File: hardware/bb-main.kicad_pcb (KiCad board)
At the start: 2 copper layers, 62 x 19 mm, 27 parts, among them P1 USB_B, P2 PICkit3, P3 OLED, SW1 SW_PUSH, U1 BU33TD3WG-TR, U2 PIC16(L)F1455-I/SL

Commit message: Board rework
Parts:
- added ?: , Housings_Proj:VIA-0.6mm, F.Cu at (91.2, 77.5)
- C1, C3, C4: footprint Capacitors_SMD:C_0603_HandSoldering -> Capacitors_SMD:C_0603
- C2: footprint Capacitors_Tantalum_SMD:TantalC_SizeA_EIA-3216_HandSoldering -> Capacitors_Tantalum_SMD:TantalC_SizeA_EIA-3216_Reflow
- D2: value L1 -> Led_Small
- moved R9 17.5 mm to (93.7, 72.1), turned to 0 degrees
- moved R1 17.3 mm to (80.3, 73.9), turned to 0 degrees
- moved R13 17.2 mm to (93.7, 77.5), turned to 0 degrees
- moved R12 16.2 mm to (93.7, 70.4), turned to 0 degrees
- moved R10 16.1 mm to (93.7, 75.7), turned to 0 degrees
- moved R11 16.1 mm to (93.7, 73.9), turned to 0 degrees
- moved SW1 14.4 mm to (85.1, 84.3)
- moved D1 13.7 mm to (66.1, 84.6)
- moved R5 13.5 mm to (93.7, 86.6)
- moved P2 13.0 mm to (81.0, 71.1), turned to 180 degrees
- moved R3 11.4 mm to (69.8, 84.6), turned to 180 degrees
- moved D2 8.86 mm to (57.7, 74.7), turned to 270 degrees
- moved R4 8.48 mm to (93.7, 79.5)
- moved R6 6.23 mm to (93.7, 81.3)
- moved R3.2 6.10 mm to (59.4, 74.1)
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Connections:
- P1 pad 5: Net-(P1-Pad5) -> (no net)
- P2 pad 6: Net-(P2-Pad6) -> (no net)
- P3 pad 5: GND -> /~RES~
- P3 pad 6: GND -> /~CS~
- P3 pad 7: /~RES~ -> GND
- P3 pad 8: /~CS~ -> GND
- U1 pad 4: Net-(U1-Pad4) -> (no net)
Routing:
- net +5V: track 0.71 -> 60.8 mm, vias 0 -> 2
- net +3V3: track 0.39 -> 51.0 mm, vias 0 -> 1
- net /ICSPDAT/OLED_SCK: track 0.45 -> 34.3 mm
- net /OLED_SDO: track 0.15 -> 25.5 mm, vias 0 -> 2
- net /OLED_~RES~: track 0.00 -> 20.4 mm
- net /OLED_D/~C~: track 0.15 -> 20.0 mm
- net /OLED_~CS~: track 1.15 -> 20.2 mm
- net /BUT_1: track 0.00 -> 16.7 mm
- net /SCK: track 13.5 -> 30.1 mm
- net /~RES~: track 13.7 -> 26.4 mm
- net /~MCLR~: track 1.92 -> 11.6 mm, vias 0 -> 2
- net GND: track 21.9 -> 13.2 mm, vias 2 -> 0
- net /LED_A: track 0.00 -> 7.69 mm
- net /SDO: track 13.5 -> 6.92 mm, vias 0 -> 1
- net /ICSPCLK: track 0.60 -> 6.77 mm
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- added copper zone on B.Cu, net GND
- added copper zone on F.Cu, net GND
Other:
- board size 62 x 19 mm -> 50.5 x 19 mm
- board text added: "Devs Build Button"
- board text added: "v1.0"

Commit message: Board changes
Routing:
- net /SDO: track 6.92 -> 8.95 mm
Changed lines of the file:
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@@
   (general
     (links 56)
-    (no_connects 15)
-    (area 54.949999 68.949999 105.550001 88.050001)
+    (no_connects 1)
+    (area 53.852999 68.949999 105.550001 88.413001)
     (thickness 1.6)
     (drawings 7)
-    (tracks 171)
+    (tracks 172)
     (zones 0)
     (modules 28)
@@
     (47 F.CrtYd user)
     (48 B.Fab user)
-    (49 F.Fab user)
+    (49 F.Fab user hide)
   )
   (setup
@@
       (net 1 GND) (zone_connect 2))
   )
-  (gr_text v1.0 (at 89.662 71.628) (layer F.Cu)
+  (gr_text v1.0 (at 91.694 67.183) (layer F.Cu)
     (effects (font (size 0.508 0.508) (thickness 0.127)))
   )
-  (gr_text "Devs Build Button" (at 86.995 70.485) (layer F.Cu)
+  (gr_text "Devs Build Button" (at 86.995 67.056) (layer F.Cu)
     (effects (font (size 1.27 0.508) (thickness 0.127)))
   )
@@
   (segment (start 68.207 78.46) (end 68.94 78.46) (width 0.254) (layer F.Cu) (net 2))
   (segment (start 68.94 78.46) (end 69.944 78.46) (width 0.254) (layer F.Cu) (net 2))
+  (segment (start 71.9582 73.025) (end 64.516 80.4672) (width 0.381) (layer B.Cu) (net 3))
   (segment (start 67.25751 69.71349) (end 65.278 71.693) (width 0.381) (layer F.Cu) (net 3))
   (segment (start 76.7334 73.025) (end 71.9582 73.025) (width 0.381) (layer B.Cu) (net 3))
-  (segment (start 71.9582 73.025) (end 64.516 80.4672) (width 0.381) (layer B.Cu) (net 3))
   (segment (start 78.486 71.2724) (end 76.7334 73.025) (width 0.381) (layer B.Cu) (net 3))
   (segment (start 78.486 71.2724) (end 78.486 71.12) (width 0.381) (layer B.Cu) (net 3))
@@
   (segment (start 70.866 71.2724) (end 70.866 71.12) (width 0.254) (layer F.Cu) (net 11))
   (segment (start 72.001001 72.407401) (end 70.866 71.2724) (width 0.254) (layer F.Cu) (net 11))
+  (segment (start 94.826 77.47) (end 94.826 79.502) (width 0.254) (layer F.Cu) (net 12))
   (segment (start 96.266 77.47) (end 99.06 74.676) (width 0.254) (layer B.Cu) (net 12))
   (segment (start 99.06 74.676) (end 100.584 74.676) (width 0.254) (layer B.Cu) (net 12))

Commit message: Board final rev 1.0
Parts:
- removed ?: , Housings_Proj:VIA-0.6mm
- moved R9 18.1 mm to (82.8, 86.6), turned to 180 degrees
- moved R5 17.1 mm to (77.5, 81.3)
- moved R6 16.4 mm to (77.5, 83.1)
- moved R8 16.4 mm to (77.5, 86.6)
- moved R7 16.4 mm to (77.5, 84.8)
- moved R4 16.3 mm to (77.5, 79.5)
- moved R12 15.4 mm to (82.8, 81.3), turned to 180 degrees
- moved R10 14.2 mm to (82.8, 84.8), turned to 180 degrees
- moved R11 14.2 mm to (82.8, 83.1), turned to 180 degrees
- moved R13 14.1 mm to (79.7, 77.7), turned to 180 degrees
- moved OLED 13.6 mm to (95.0, 85.6), turned to 180 degrees
- moved BTN 11.9 mm to (92.5, 74.9), turned to 90 degrees
- moved R3.2 6.72 mm to (65.5, 71.2)
- moved C2 6.37 mm to (58.6, 75.1)
- moved D2 6.31 mm to (63.9, 73.7)
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- renumbered SW1 to BTN, P3 to OLED, P1 to USB
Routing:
- net GND: track 13.2 -> 47.9 mm
- net /BUT_1: track 16.7 -> 32.7 mm, vias 0 -> 1
- net /ICSPDAT/OLED_SCK: track 34.3 -> 20.0 mm, vias 0 -> 1
- net /~RES~: track 26.4 -> 13.6 mm, vias 0 -> 1
- net /OLED_SDO: track 25.5 -> 14.4 mm, vias 2 -> 0
- net /SDO: track 8.95 -> 19.7 mm
- net /OLED_D/~C~: track 20.0 -> 9.83 mm
- net /OLED_~CS~: track 20.2 -> 10.3 mm
- net +5V: track 60.8 -> 50.9 mm, vias 2 -> 3
- net /OLED_~RES~: track 20.4 -> 10.8 mm
- net /~MCLR~: track 11.6 -> 16.6 mm, vias 2 -> 1
- net /SCK: track 30.1 -> 35.1 mm, vias 0 -> 1
- net Net-(P1-Pad3): track 8.00 -> 5.33 mm
- net Net-(P1-Pad2): track 8.19 -> 5.52 mm
- net /D/~C~: track 14.6 -> 16.6 mm, vias 0 -> 1
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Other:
- board size 50.5 x 19 mm -> 41.9 x 19 mm
- net class Default: trace_width 0.254 -> 0.2032
- net class Power: trace_width 0.381 -> 0.254
- rule via_min_size: 0.4 -> 0.3302
- board text added: "Button"
- board text added: "Devs Build"
- board text removed: "Devs Build Button"

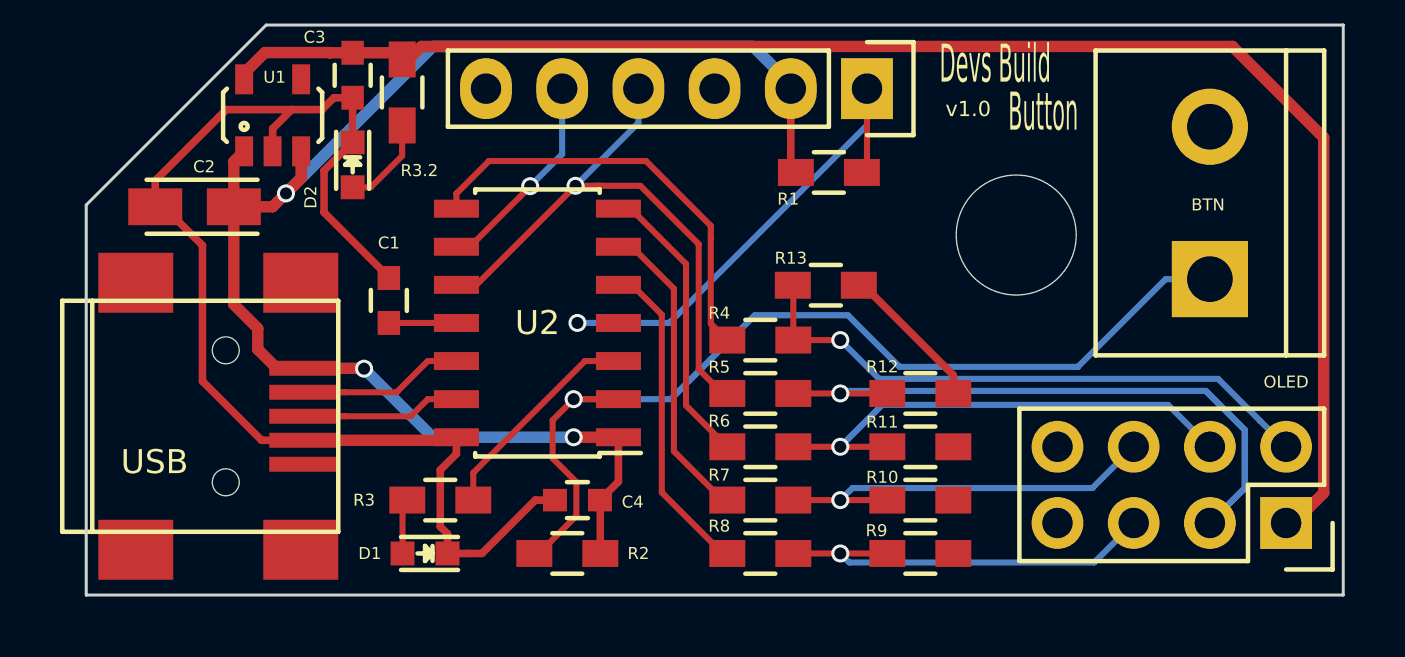
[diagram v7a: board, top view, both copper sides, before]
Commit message: Fix board unconnected track. Changed schematic USB connector.
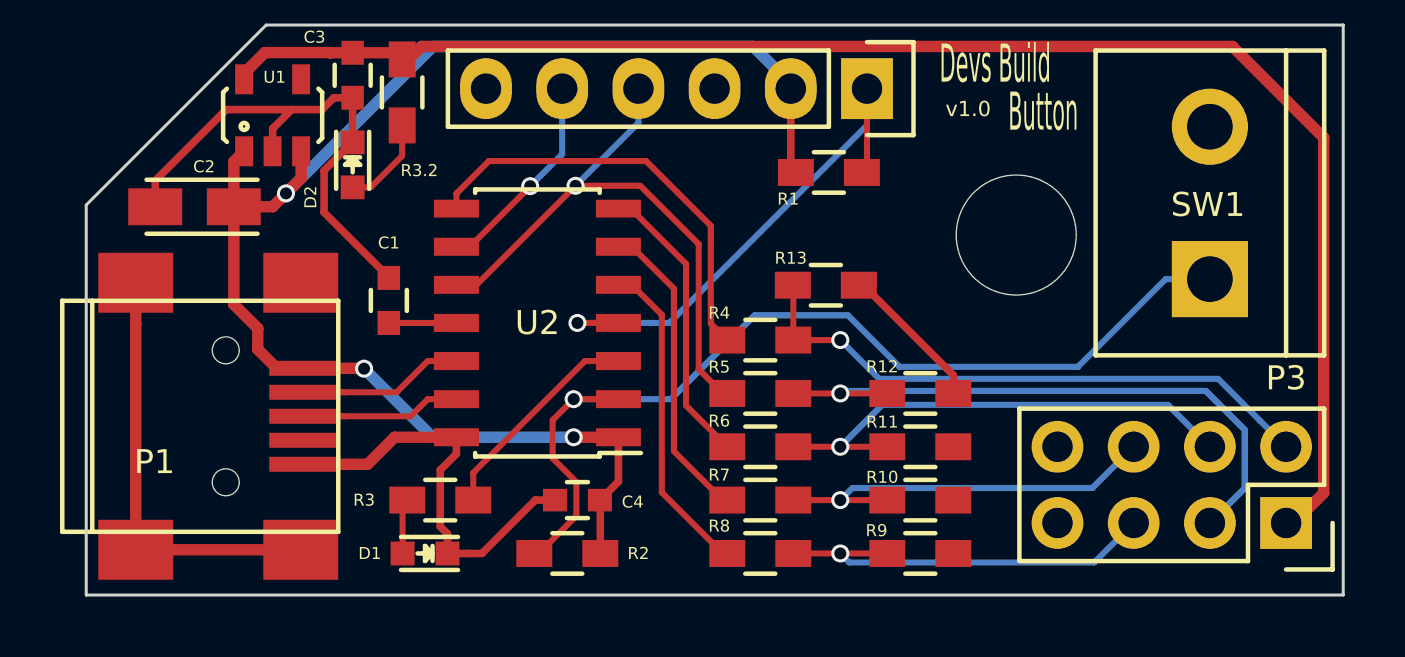
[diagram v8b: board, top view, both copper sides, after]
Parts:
- renumbered USB to P1, OLED to P3, BTN to SW1
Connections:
- P1 pad 4: GND -> Net-(P1-Pad4)
- P1 pad 5: (no net) -> GND
- P1 pad 6: (no net) -> GND
- P2 pad 6: (no net) -> Net-(P2-Pad6)
- U1 pad 4: (no net) -> Net-(U1-Pad4)
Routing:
- net GND: track 47.9 -> 52.3 mm
- net /~MCLR~: track 16.6 -> 18.0 mm
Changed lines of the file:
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@@
-(kicad_pcb (version 4) (host pcbnew 4.0.2-stable)
+(kicad_pcb (version 4) (host pcbnew 4.0.0-stable)
   (general
-    (links 55)
-    (no_connects 0)
-    (area 53.725999 68.090976 96.971001 88.050001)
+    (links 59)
+    (no_connects 11)
+    (area 54.949999 68.949999 96.951001 88.050001)
     (thickness 1.6)
     (drawings 8)
-    (tracks 208)
+    (tracks 210)
     (zones 0)
     (modules 27)
-    (nets 23)
+    (nets 26)
   )
   (page A4)
@@
   )
   (setup
-    (last_trace_width 0.2032)
+    (last_trace_width 0.381)
     (user_trace_width 0.2032)
     (user_trace_width 0.254)
@@
   (net 21 /OLED_~CS~)
   (net 22 /OLED_~RES~)
+  (net 23 "Net-(P1-Pad4)")
+  (net 24 "Net-(P2-Pad6)")
+  (net 25 "Net-(U1-Pad4)")
   (net_class Default "This is the default net class."
     (clearance 0.2)
@@
     (add_net "Net-(P1-Pad2)")
     (add_net "Net-(P1-Pad3)")
+    (add_net "Net-(P1-Pad4)")
+    (add_net "Net-(P2-Pad6)")
+    (add_net "Net-(U1-Pad4)")
   )
   (net_class Power ""
@@
     (descr "Through hole socket strip")
     (tags "socket strip")
-    (fp_text reference OLED (at 0 4.699 180) (layer F.SilkS)
-      (effects (font (size 0.4 0.4) (thickness 0.07)))
+    (fp_text reference P3 (at 0 4.826 180) (layer F.SilkS)
+      (effects (font (size 0.8 0.8) (thickness 0.1)))
     )
     (fp_text value OLED (at 10.16 1.27 270) (layer F.Fab)
@@
     (descr "Bornier d'alimentation 2 pins")
     (tags DEV)
-    (fp_text reference BTN (at -0.0635 -0.0635 180) (layer F.SilkS)
-      (effects (font (size 0.4 0.4) (thickness 0.07)))
+    (fp_text reference SW1 (at -0.0635 -0.0635 180) (layer F.SilkS)
+      (effects (font (size 0.8 0.8) (thickness 0.1)))
     )
     (fp_text value SW_PUSH (at -0.254 2.286 90) (layer F.Fab)
@@
     (tags "USB USB_B USB_Mini connector")
     (attr smd)
-    (fp_text reference USB (at -1.524 1.524) (layer F.SilkS)
-      (effects (font (size 0.8 0.8) (thickness 0.08)))
+    (fp_text reference P1 (at -1.524 1.524) (layer F.SilkS)
+      (effects (font (size 0.8 0.8) (thickness 0.1)))
     )
     (fp_text value USB_B (at -0.762 -0.508 180) (layer F.Fab)
@@
       (net 8 "Net-(P1-Pad3)"))
     (pad 4 smd rect (at 3.44932 0.8001) (size 2.30124 0.50038) (layers F.Cu F.Paste F.Mask)
-      (net 1 GND))
-    (pad 5 smd rect (at 3.44932 1.6002) (size 2.30124 0.50038) (layers F.Cu F.Paste F.Mask))
-    (pad 6 smd rect (at 3.35026 -4.45008) (size 2.49936 1.99898) (layers F.Cu F.Paste F.Mask))
-    (pad 6 smd rect (at -2.14884 -4.45008) (size 2.49936 1.99898) (layers F.Cu F.Paste F.Mask))
-    (pad 6 smd rect (at 3.35026 4.45008) (size 2.49936 1.99898) (layers F.Cu F.Paste F.Mask))
-    (pad 6 smd rect (at -2.14884 4.45008) (size 2.49936 1.99898) (layers F.Cu F.Paste F.Mask))
+      (net 23 "Net-(P1-Pad4)"))
+    (pad 5 smd rect (at 3.44932 1.6002) (size 2.30124 0.50038) (layers F.Cu F.Paste F.Mask)
+      (net 1 GND))
+    (pad 6 smd rect (at 3.35026 -4.45008) (size 2.49936 1.99898) (layers F.Cu F.Paste F.Mask)
+      (net 1 GND))
+    (pad 6 smd rect (at -2.14884 -4.45008) (size 2.49936 1.99898) (layers F.Cu F.Paste F.Mask)
+      (net 1 GND))
+    (pad 6 smd rect (at 3.35026 4.45008) (size 2.49936 1.99898) (layers F.Cu F.Paste F.Mask)
+      (net 1 GND))
+    (pad 6 smd rect (at -2.14884 4.45008) (size 2.49936 1.99898) (layers F.Cu F.Paste F.Mask)
+      (net 1 GND))
     (pad "" np_thru_hole circle (at 0.8509 -2.19964) (size 0.89916 0.89916) (drill 0.89916) (layers *.Cu *.Mask F.SilkS))
     (pad "" np_thru_hole circle (at 0.8509 2.19964) (size 0.89916 0.89916) (drill 0.89916) (layers *.Cu *.Mask F.SilkS))
@@
     (pad 5 thru_hole oval (at 10.16 0 180) (size 1.7272 2.032) (drill 1.016) (layers *.Cu *.Mask F.SilkS)
       (net 11 /ICSPCLK))
-    (pad 6 thru_hole oval (at 12.7 0 180) (size 1.7272 2.032) (drill 1.016) (layers *.Cu *.Mask F.SilkS))
+    (pad 6 thru_hole oval (at 12.7 0 180) (size 1.7272 2.032) (drill 1.016) (layers *.Cu *.Mask F.SilkS)
+      (net 24 "Net-(P2-Pad6)"))
     (model Socket_Strips.3dshapes/Socket_Strip_Straight_1x06.wrl
       (at (xyz 0.25 0 0))
@@
     (pad 2 smd rect (at 0 1.2) (size 0.6 1) (layers F.Cu F.Paste F.Mask)
       (net 1 GND))
-    (pad 4 smd rect (at 0.95 -1.2) (size 0.6 1) (layers F.Cu F.Paste F.Mask))
+    (pad 4 smd rect (at 0.95 -1.2) (size 0.6 1) (layers F.Cu F.Paste F.Mask)
+      (net 25 "Net-(U1-Pad4)"))
     (pad 3 smd rect (at 0.95 1.2) (size 0.6 1) (layers F.Cu F.Paste F.Mask)
       (net 3 +5V))
@@
   (gr_line (start 55 75) (end 55 88) (angle 90) (layer Edge.Cuts) (width 0.1))
   (gr_line (start 55 75) (end 61 69) (angle 90) (layer Edge.Cuts) (width 0.1))
+  (segment (start 64.3763 83.6422) (end 65.278 82.7405) (width 0.381) (layer F.Cu) (net 1))
+  (segment (start 65.278 82.7405) (end 67.3405 82.7405) (width 0.381) (layer F.Cu) (net 1))
+  (segment (start 62.25032 83.6422) (end 64.3763 83.6422) (width 0.381) (layer F.Cu) (net 1))
   (segment (start 80.7544 77.6732) (end 80.9044 77.6732) (width 0.254) (layer F.Cu) (net 1))
   (segment (start 80.9044 77.6732) (end 83.904 80.6728) (width 0.254) (layer F.Cu) (net 1))
   (segment (start 83.904 80.6728) (end 83.904 81.28) (width 0.254) (layer F.Cu) (net 1))
-  (segment (start 62.25032 82.8421) (end 67.2389 82.8421) (width 0.381) (layer F.Cu) (net 1))
   (segment (start 67.2389 82.8421) (end 67.3405 82.7405) (width 0.381) (layer F.Cu) (net 1))
   (segment (start 62.9285 73.8505) (end 62.9285 75.2465) (width 0.254) (layer F.Cu) (net 1))
@@
   (segment (start 66.8905 82.7405) (end 67.3405 82.7405) (width 0.254) (layer F.Cu) (net 1))
   (segment (start 57.3005 75.057) (end 57.5855 75.057) (width 0.254) (layer F.Cu) (net 1))
-  (segment (start 57.5855 75.057) (end 58.875319 76.346819) (width 0.254) (layer F.Cu) (net 1))
-  (segment (start 58.875319 76.346819) (end 58.875319 80.871719) (width 0.254) (layer F.Cu) (net 1))
-  (segment (start 58.875319 80.871719) (end 60.8457 82.8421) (width 0.254) (layer F.Cu) (net 1))
-  (segment (start 60.8457 82.8421) (end 62.25032 82.8421) (width 0.254) (layer F.Cu) (net 1))
   (segment (start 65.0875 77.4305) (end 65.0875 77.4555) (width 0.254) (layer F.Cu) (net 1))
   (segment (start 61.8505 71.8185) (end 59.67 71.8185) (width 0.254) (layer F.Cu) (net 1))
@@
   (segment (start 63.252 71.4255) (end 62.859 71.8185) (width 0.254) (layer F.Cu) (net 1))
   (segment (start 63.881 72.9107) (end 63.881 71.4255) (width 0.254) (layer F.Cu) (net 1))
+  (segment (start 56.65216 86.49208) (end 62.15126 86.49208) (width 0.381) (layer F.Cu) (net 1))
+  (segment (start 56.65216 77.59192) (end 56.65216 78.97241) (width 0.381) (layer F.Cu) (net 1))
+  (segment (start 56.65216 78.97241) (end 56.65216 86.49208) (width 0.381) (layer F.Cu) (net 1))
   (segment (start 65.0875 78.9305) (end 67.3405 78.9305) (width 0.2032) (layer F.Cu) (net 2))
   (segment (start 78.486 71.12) (end 78.486 73.744) (width 0.254) (layer F.Cu) (net 3))
@@
   (segment (start 65.8158 82.042) (end 63.60414 82.042) (width 0.2032) (layer F.Cu) (net 8))
   (segment (start 63.60414 82.042) (end 62.25032 82.042) (width 0.2032) (layer F.Cu) (net 8))
+  (segment (start 71.374 78.9305) (end 72.7405 78.9305) (width 0.2032) (layer F.Cu) (net 9))
   (segment (start 81.026 72.3392) (end 74.4347 78.9305) (width 0.2032) (layer B.Cu) (net 9))
   (segment (start 81.026 71.12) (end 81.026 72.3392) (width 0.2032) (layer B.Cu) (net 9))
